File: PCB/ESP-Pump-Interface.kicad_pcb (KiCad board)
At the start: 2 copper layers, 28.6 x 52.1 mm, 24 parts, among them J1 USB_C_Receptacle_PowerOnly_6P, Q1 2N2219, Q2 2N2219, Q3 2N2219, Q4 2N2219, U1 DOIT-ESP32-DEVKIT-V1

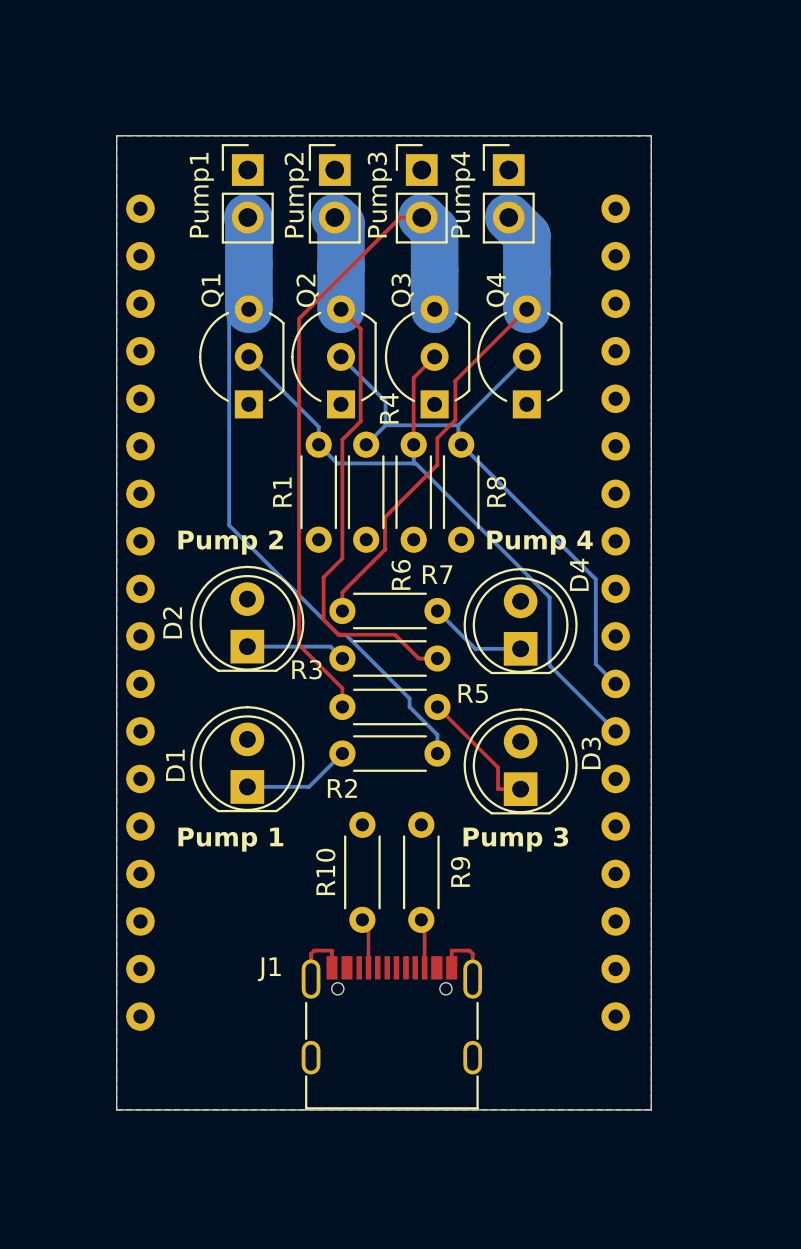
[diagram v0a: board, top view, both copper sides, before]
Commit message: changed esp32-doit-devkit V1 symbol and footprint (source: SNAPEDA)
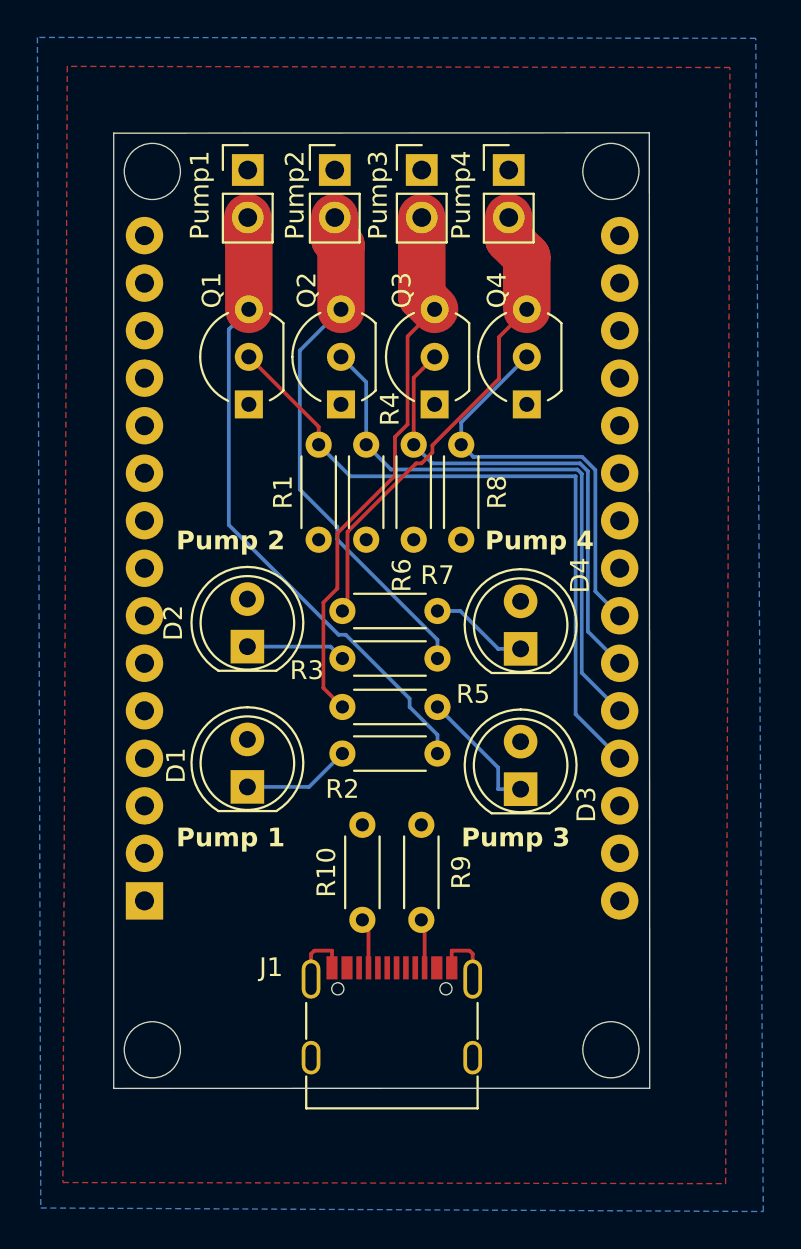
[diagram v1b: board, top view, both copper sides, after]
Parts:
- U1: footprint doit-esp32-devkit-kicad-master:ESP32-DOIT-DEVKIT -> ESP32-DEVKIT-V1:MODULE_ESP32_DEVKIT_V1
- moved U1 24.0 mm to (141.2, 69.8), turned to 0 degrees
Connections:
- Q3 pad 2: Pump1 -> Pump3
- Q4 pad 2: Pump2 -> Pump4
- R6 pad 1: Pump1 -> Pump3
- R8 pad 1: Pump2 -> Pump4
- U1 pad 10: Pump3 -> unconnected-(U1-D19-Pad10)
- U1 pad 11: Pump2 -> unconnected-(U1-D21-Pad11)
- U1 pad 12: Pump1 -> unconnected-(U1-RX0-Pad12)
- U1 pad 17: GND -> unconnected-(U1-VP-Pad17)
- U1 pad 18: +5V -> unconnected-(U1-VN-Pad18)
- U1 pad 2: unconnected-(U1-GPIO36_ADC-CH0_SENS-VP_RTC-GPIO0-Pad2) -> GND
- U1 pad 24: unconnected-(U1-GPIO15_ADC2-CH3_HSPI-CS0_RTC-GPIO13-Pad24) -> Pump4
- U1 pad 25: unconnected-(U1-GPIO2_ADC2-CH2_RTC-GPIO12-Pad25) -> Pump3
- U1 pad 26: unconnected-(U1-GPIO4_ADC2-CH0_RTC-GPIO10-Pad26) -> Pump2
- U1 pad 27: unconnected-(U1-GPIO16_UART2-RX-Pad27) -> Pump1
- U1 pad 29: unconnected-(U1-GPIO5_VSPI-CS0-Pad29) -> GND
- U1 pad 30: unconnected-(U1-GPIO18_VSPI-CLK-Pad30) -> +5V
- U1 pad 9: Pump4 -> unconnected-(U1-D18-Pad9)
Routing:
- net Pump3: track 0.00 -> 26.0 mm
- net Pump4: track 0.00 -> 22.2 mm
- net Net-(Pump3-Pin_2): track 37.8 -> 29.3 mm
- net Net-(Pump2-Pin_2): track 32.1 -> 27.7 mm
- net Net-(Pump1-Pin_2): track 36.9 -> 34.0 mm
- net Net-(Pump4-Pin_2): track 27.5 -> 25.7 mm
- net Pump2: track 32.5 -> 30.9 mm
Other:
- board size 28.6 x 52.1 mm -> 28.7 x 51.1 mm
